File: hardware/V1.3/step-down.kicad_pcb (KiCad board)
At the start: 2 copper layers, 40 x 40 mm, 37 parts, among them J1 STACK-UP-HIGH, J2 STACK-UP-HIGH, P1 Black, P2 Green, Q1 FDS8449, U1 ZXCT1086, U2 AOZ1212, U3 DRILL, U4 DRILL, U5 DRILL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

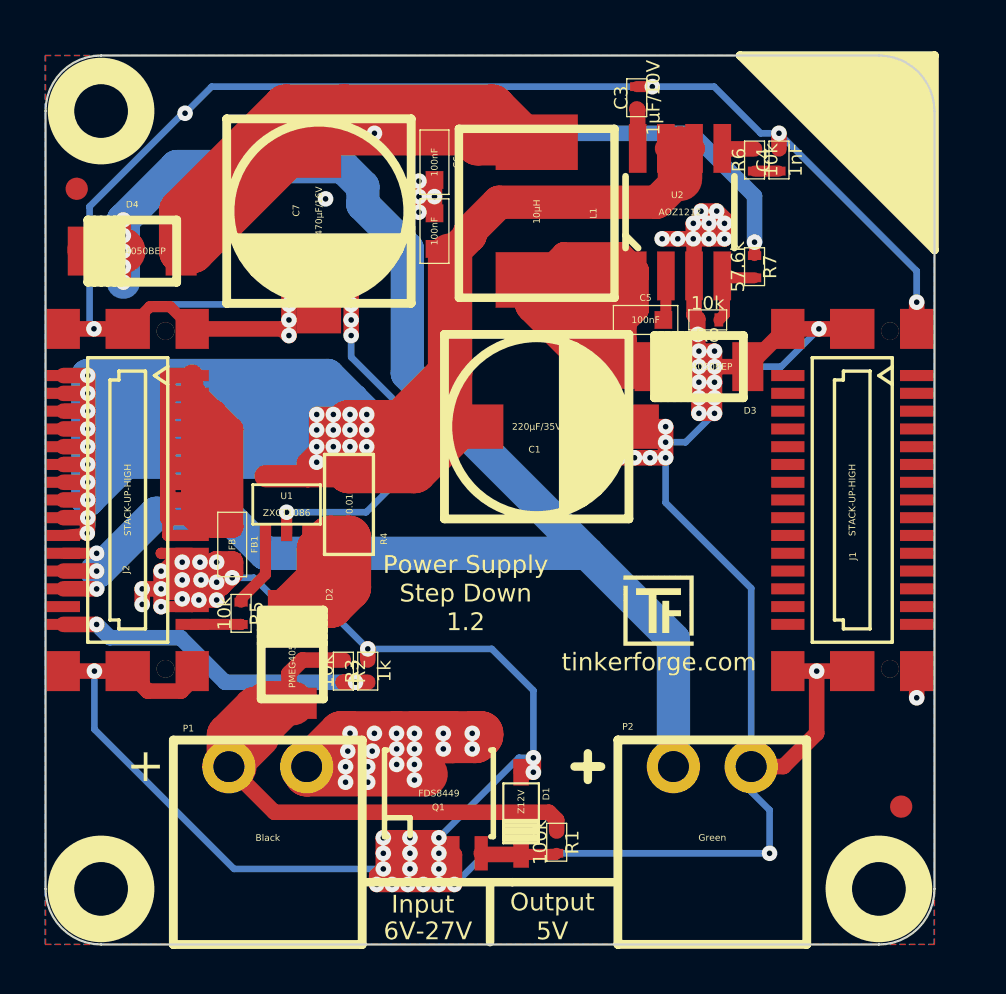
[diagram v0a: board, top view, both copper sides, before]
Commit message: updated version of new prototype, change current sensor, add filtering, not finished
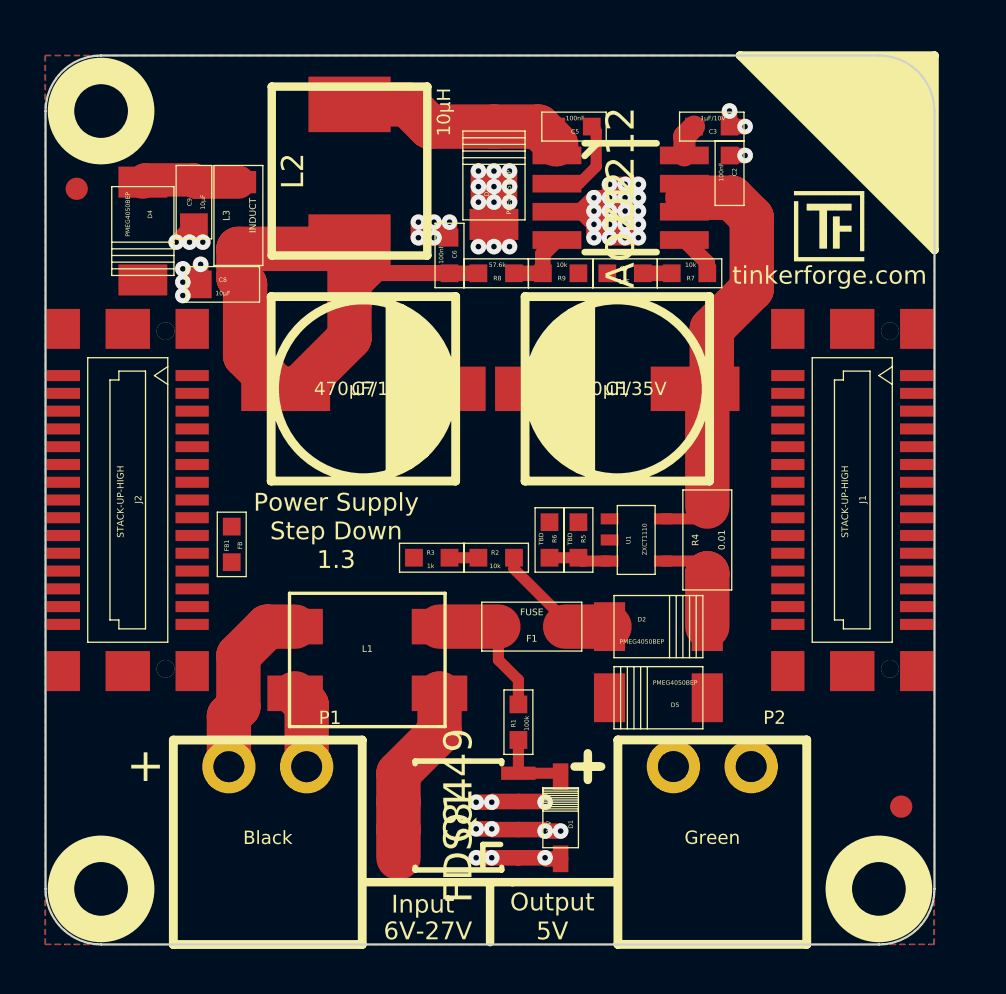
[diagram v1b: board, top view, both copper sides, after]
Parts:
- added C8: 10µF, kicad-libraries:0805, F.Cu at (138.6, 93.9)
- added C9: 10µF, kicad-libraries:0805, F.Cu at (137.3, 90.2)
- added D5: PMEG4050BEP, kicad-libraries:SOD-128, F.Cu at (158.2, 112.5)
- added F1: FUSE, kicad-libraries:1206, F.Cu at (152.5, 109.3)
- added L2: 10µH, kicad-libraries:SRP7030, F.Cu at (144.3, 88.9)
- added L3: INDUCT, kicad-libraries:1206, F.Cu at (139.3, 90.8)
- added R9: 10k, kicad-libraries:0603, F.Cu at (153.8, 93.4)
- C1, C7: footprint ELKO_83 -> kicad-libraries:ELKO_83
- C2, C5, C6, FB1: footprint 0603 -> kicad-libraries:0603
- C3, C4, R1, R2, R3: footprint 0402 -> kicad-libraries:0603
- D1: footprint SOD-123 -> kicad-libraries:SOD-123
- D2, D3, D4: footprint SOD-128 -> kicad-libraries:SOD-128
- J1, J2: footprint BTB08-ACS-TOP -> kicad-libraries:BTB08-ACS-TOP
- L1: value 10µH -> ICM2824ER301V; footprint SRP7030 -> kicad-libraries:ICM2824
- P1, P2: footprint OQ_2P -> kicad-libraries:OQ_2P
- Q1: footprint SOIC-8-MOSFET -> kicad-libraries:SOIC-8-MOSFET
- R4: footprint 1206 -> kicad-libraries:1206
- R5, R6: value 10k -> TBD; footprint 0402 -> kicad-libraries:0603
- R7: value 57.6k -> 10k; footprint 0402 -> kicad-libraries:0603
- R8: value 10k -> 57.6k; footprint 0402 -> kicad-libraries:0603
- U1: value ZXCT1086 -> ZXCT1110; footprint SOT23-5 -> kicad-libraries:SOT23-5
- U2: footprint SO-8 -> kicad-libraries:SO-8
- U3, U4, U5, U6: footprint DRILL_NP -> kicad-libraries:DRILL_NP
- moved L1 21.6 mm to (145.1, 110.8), turned to 180 degrees
- moved R6 19.4 mm to (153.3, 105.4)
- moved Ref** 18.9 mm to (164.3, 89.7)
- moved D2 16.5 mm to (158.2, 109.3), turned to 180 degrees
- moved R4 16.2 mm to (160.4, 105.4)
- moved U1 15.8 mm to (157.2, 105.4), turned to 270 degrees
- moved R5 15.5 mm to (154.6, 105.4), turned to 90 degrees
- moved C2 13.5 mm to (161.4, 88.9)
- moved D3 12.6 mm to (150.8, 89.0), turned to 270 degrees
- moved R8 9.75 mm to (150.9, 93.4), turned to 0 degrees
- moved C5 9.28 mm to (154.4, 86.8)
- moved C4 8.60 mm to (156.7, 93.4), turned to 180 degrees
- moved R2 8.56 mm to (150.9, 106.2), turned to 180 degrees
- moved C7 8.24 mm to (144.9, 98.6), turned to 180 degrees
- moved R3 5.86 mm to (148.0, 106.2), turned to 180 degrees
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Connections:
- C4 pad 1: N-000015 -> Net-(C4-Pad1)
- C5 pad 1: N-000005 -> Net-(C5-Pad1)
- C6 pad 1: N-000007 -> Net-(C6-Pad1)
- C7 pad 1: N-000007 -> Net-(C6-Pad1)
- D2 pad 1: N-000017 -> Net-(D2-Pad1)
- D2 pad 2: N-000002 -> Net-(D2-Pad2)
- D3 pad 2: N-000005 -> Net-(C5-Pad1)
- D4 pad 1: N-000007 -> Net-(C9-Pad1)
- L1 pad 1: N-000005 -> Net-(L1-Pad1)
- L1 pad 2: N-000007 -> Net-(L1-Pad2)
- P1 pad 1: N-000017 -> Net-(L1-Pad3)
- P1 pad 2: N-000012 -> Net-(L1-Pad2)
- P2 pad 1: +5V -> Net-(D5-Pad2)
- Q1 pad D: N-000012 -> Net-(L1-Pad1)
- R1 pad 1: N-000017 -> Net-(F1-Pad1)
- R2 pad 1: N-000017 -> Net-(D2-Pad1)
- R4 pad 2: N-000002 -> Net-(D2-Pad2)
- R5 pad 1: N-000004 -> Net-(R5-Pad1)
- R5 pad 2: CURRENT -> GND
- R6 pad 1: N-000015 -> Net-(R5-Pad1)
- R6 pad 2: N-000016 -> CURRENT
- R7 pad 1: N-000007 -> Net-(C4-Pad1)
- R7 pad 2: N-000010 -> Net-(R7-Pad2)
- R8 pad 1: N-000010 -> Net-(C6-Pad1)
- R8 pad 2: GND -> Net-(R8-Pad2)
- U1 pad 1: N-000004 -> (no net)
- U1 pad 3: N-000002 -> Net-(R5-Pad1)
- U1 pad 4: VPP -> Net-(D2-Pad2)
- U2 pad 1: N-000005 -> Net-(C5-Pad1)
- U2 pad 4: N-000010 -> Net-(R8-Pad2)
- U2 pad 5: N-000016 -> Net-(R7-Pad2)
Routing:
- net GND: track 289.4 -> 51.8 mm, vias 92 -> 57
- net VPP: track 158.0 -> 22.8 mm, vias 23 -> 0
- net +5V: track 84.6 -> 0.00 mm, vias 8 -> 0
- net N-000007: track 68.3 -> 0.00 mm, vias 2 -> 0
- net N-000012: track 52.6 -> 0.00 mm, vias 19 -> 0
- net AGND: track 42.4 -> 0.00 mm
- net N-000017: track 36.1 -> 0.00 mm
- net Net-(C6-Pad1): track 0.00 -> 32.0 mm
- net N-000005: track 28.3 -> 0.00 mm
- net VOLTAGE: track 16.4 -> 1.30 mm, vias 2 -> 0
- net Net-(C5-Pad1): track 0.00 -> 14.2 mm
- net N-000002: track 11.7 -> 0.00 mm
- net Net-(L1-Pad3): track 0.00 -> 8.27 mm
- net Net-(L1-Pad1): track 0.00 -> 8.17 mm
- net Net-(F1-Pad1): track 0.00 -> 6.52 mm
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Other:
- board text added: "Power Supply Step Down 1.3"
- board text removed: "Power Supply Step Down 1.2"

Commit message: next routing test, vpp seems to be not routable
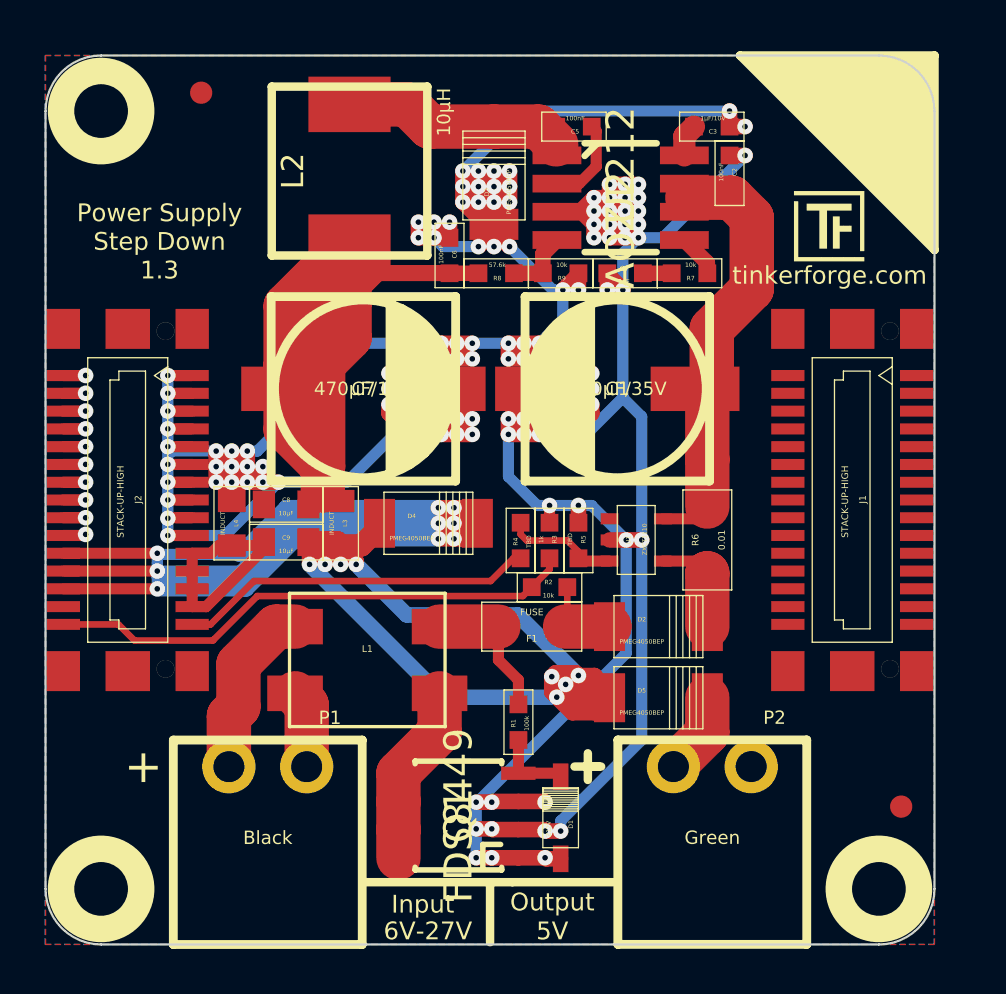
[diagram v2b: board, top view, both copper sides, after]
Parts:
- removed FB1: FB, kicad-libraries:0603
- added L4: INDUCT, kicad-libraries:0805, F.Cu at (139.0, 104.7)
- L3: footprint kicad-libraries:1206 -> kicad-libraries:0805
- R4: value 0.01 -> TBD; footprint kicad-libraries:1206 -> kicad-libraries:0603
- R6: value TBD -> 0.01; footprint kicad-libraries:0603 -> kicad-libraries:1206
- moved D4 18.4 mm to (147.8, 104.7), turned to 180 degrees
- moved C9 15.9 mm to (141.4, 105.5), turned to 180 degrees
- moved L3 14.6 mm to (143.9, 104.7), turned to 90 degrees
- moved C8 10.3 mm to (141.4, 103.8)
- moved R4 8.40 mm to (152.0, 105.4)
- moved R6 7.10 mm to (160.4, 105.4), turned to 270 degrees
- moved Fiducial_Mark 7.08 mm to (137.6, 85.3)
- moved R3 5.36 mm to (153.3, 105.4), turned to 90 degrees
- moved R2 2.74 mm to (153.3, 107.5)
- turned D5 to 180 degrees
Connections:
- C1 pad 2: GND -> AGND
- C2 pad 2: GND -> AGND
- C3 pad 2: GND -> AGND
- C4 pad 2: GND -> AGND
- C6 pad 2: GND -> AGND
- C7 pad 2: GND -> AGND
- C8 pad 2: GND -> AGND
- D1 pad 1: GND -> AGND
- D3 pad 1: GND -> AGND
- J1 pad EP: GND -> AGND
- J2 pad EP: GND -> AGND
- Q1 pad S: GND -> AGND
- R3 pad 2: GND -> AGND
- R4 pad 1: VPP -> Net-(R4-Pad1)
- R4 pad 2: Net-(D2-Pad2) -> CURRENT
- R5 pad 1: Net-(R5-Pad1) -> Net-(R4-Pad1)
- R5 pad 2: GND -> AGND
- R6 pad 1: Net-(R5-Pad1) -> VPP
- R6 pad 2: CURRENT -> Net-(D2-Pad2)
- R9 pad 2: GND -> AGND
- U1 pad 2: GND -> AGND
- U1 pad 3: Net-(R5-Pad1) -> Net-(R4-Pad1)
- U2 pad 3: GND -> AGND
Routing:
- net AGND: track 0.00 -> 233.4 mm, vias 0 -> 136
- net +5V: track 0.00 -> 71.6 mm, vias 0 -> 9
- net GND: track 51.8 -> 10.4 mm, vias 57 -> 0
- net Net-(C9-Pad1): track 4.38 -> 45.2 mm, vias 0 -> 8
- net VOLTAGE: track 1.30 -> 24.0 mm
- net CURRENT: track 0.00 -> 16.7 mm
- net Net-(C6-Pad1): track 32.0 -> 43.1 mm
- net VPP: track 22.8 -> 32.8 mm, vias 0 -> 10
- net Net-(R4-Pad1): track 0.00 -> 5.21 mm
- net Net-(D5-Pad2): track 0.00 -> 3.73 mm
- net Net-(R5-Pad1): track 2.76 -> 0.00 mm
- net Net-(D2-Pad1): track 6.05 -> 4.11 mm

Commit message: routing finished
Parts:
- moved Fiducial_Mark 0.53 mm to (137.1, 85.1)
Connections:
- P2 pad 2: GND -> AGND
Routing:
- net VPP: track 32.8 -> 141.9 mm, vias 10 -> 19
- net AGND: track 233.4 -> 301.4 mm, vias 136 -> 143
- net Net-(C6-Pad1): track 43.1 -> 50.2 mm
- net +5V: track 71.6 -> 72.6 mm, vias 9 -> 11
- added copper zone on B.Cu, net +5V
- added copper zone on F.Cu, net +5V
- added copper zone on B.Cu, net AGND
- added copper zone on F.Cu, net AGND
- added copper zone on B.Cu, net Net-(C9-Pad1)
- added copper zone on B.Cu, net VPP
- added copper zone on F.Cu, net VPP
- removed copper zone on B.Cu, net GND

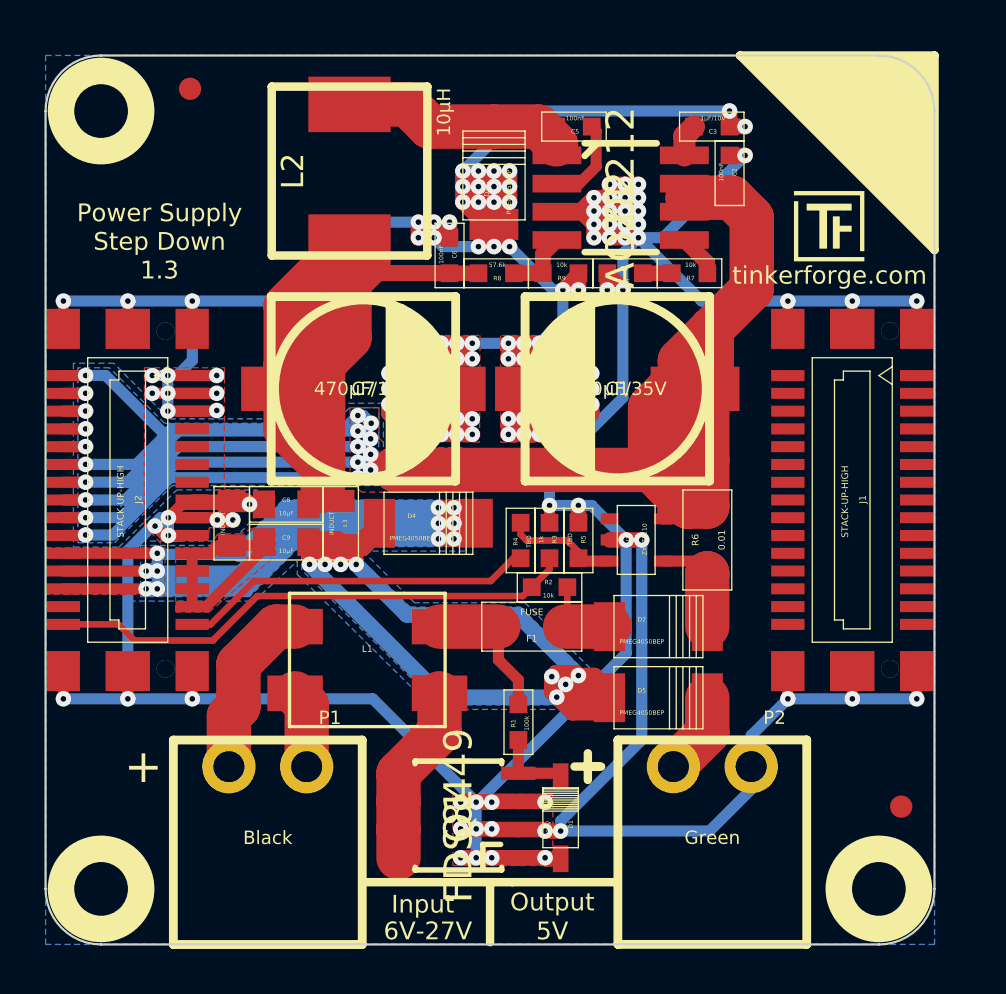
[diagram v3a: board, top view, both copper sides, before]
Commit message: change version 1.3, remove filters
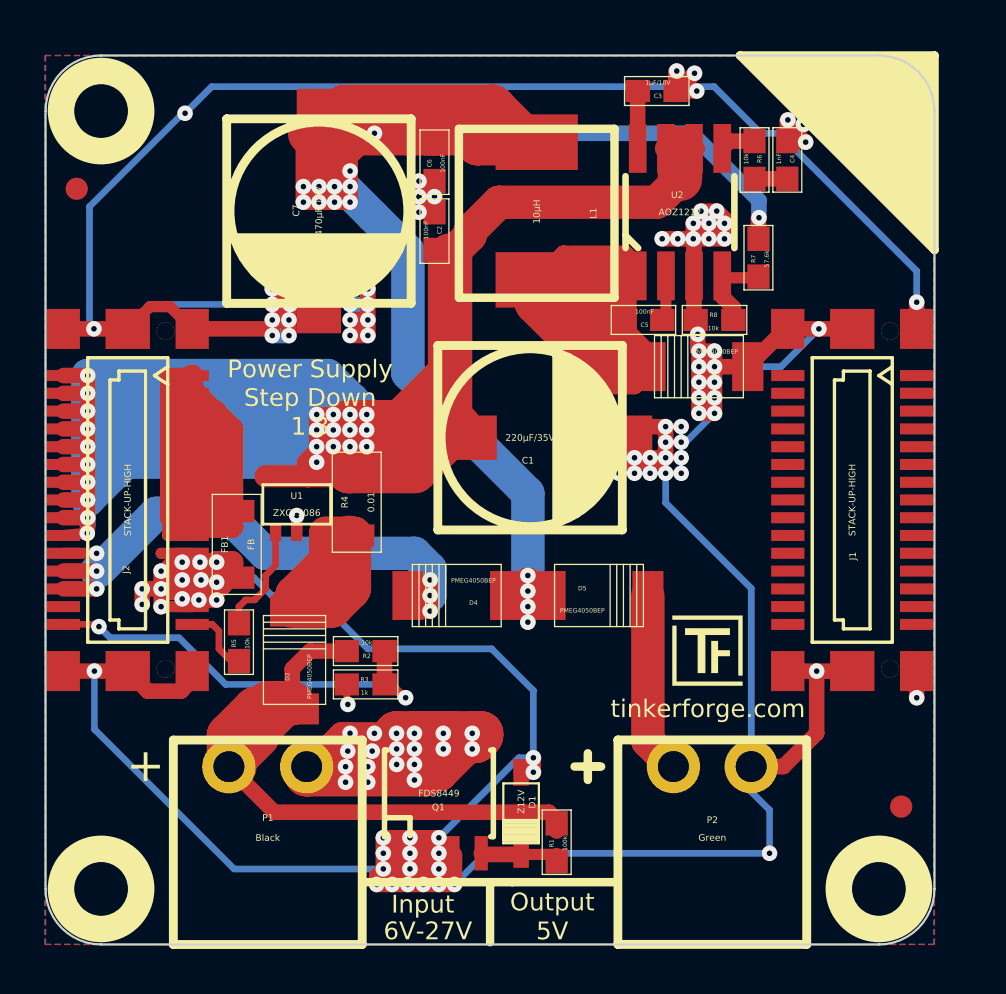
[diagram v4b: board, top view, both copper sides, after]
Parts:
- removed C8, C9: 10µF, kicad-libraries:0805
- removed F1: FUSE, kicad-libraries:1206
- removed L2: 10µH, kicad-libraries:SRP7030
- removed L3, L4: INDUCT, kicad-libraries:0805
- removed R9: 10k, kicad-libraries:0603
- added FB1: FB, kicad-libraries:1206, F.Cu at (139.2, 105.6)
- C1, C7: footprint kicad-libraries:ELKO_83 -> ELKO_83
- C2, C3, C4, C5, C6, R1, R2, R3: footprint kicad-libraries:0603 -> 0603E
- D1: footprint kicad-libraries:SOD-123 -> SOD-123
- D2, D3, D4, D5: footprint kicad-libraries:SOD-128 -> SOD-128
- J1, J2: footprint kicad-libraries:BTB08-ACS-TOP -> BTB08-ACS-TOP
- L1: value ICM2824ER301V -> 10µH; footprint kicad-libraries:ICM2824 -> SRP7030
- P1, P2: footprint kicad-libraries:OQ_2P -> OQ_2P
- Q1: footprint kicad-libraries:SOIC-8-MOSFET -> SOIC-8-MOSFET
- R4: value TBD -> 0.01; footprint kicad-libraries:0603 -> kicad-libraries:1206
- R5: value TBD -> 10k; footprint kicad-libraries:0603 -> 0603E
- R6: value 0.01 -> 10k; footprint kicad-libraries:1206 -> 0603E
- R7: value 10k -> 57.6k; footprint kicad-libraries:0603 -> 0603E
- R8: value 57.6k -> 10k; footprint kicad-libraries:0603 -> 0603E
- U1: value ZXCT1110 -> ZXCT1086; footprint kicad-libraries:SOT23-5 -> SOT23-5
- U2: footprint kicad-libraries:SO-8 -> SO-8
- U3, U4, U5, U6: footprint kicad-libraries:DRILL_NP -> DRILL_NP
- moved L1 21.6 mm to (152.7, 90.6), turned to 90 degrees
- moved Ref** 19.9 mm to (158.8, 108.8)
- moved R6 17.2 mm to (162.5, 88.3), turned to 90 degrees
- moved D2 16.4 mm to (141.8, 110.8), turned to 270 degrees
- moved R5 15.9 mm to (139.3, 110.0), turned to 270 degrees
- moved U1 15.4 mm to (141.9, 103.8), turned to 0 degrees
- moved C2 13.5 mm to (148.1, 91.5)
- moved D3 12.6 mm to (160.0, 97.6), turned to 0 degrees
- moved R3 10.5 mm to (145.0, 111.9), turned to 180 degrees
- moved R8 10.0 mm to (160.7, 95.5), turned to 180 degrees
- moved C5 9.24 mm to (157.5, 95.5)
- moved C4 8.91 mm to (164.0, 88.3), turned to 90 degrees
- moved R2 8.76 mm to (145.0, 110.4), turned to 0 degrees
- moved C7 8.24 mm to (142.9, 90.6), turned to 90 degrees
- moved R4 7.57 mm to (144.6, 103.7)
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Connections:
- C1 pad 2: AGND -> GND
- C2 pad 2: AGND -> GND
- C3 pad 2: AGND -> GND
- C4 pad 2: AGND -> GND
- C6 pad 2: AGND -> GND
- C7 pad 2: AGND -> GND
- D1 pad 1: AGND -> GND
- D3 pad 1: AGND -> GND
- D4 pad 1: Net-(C9-Pad1) -> Net-(C6-Pad1)
- D5 pad 1: Net-(C9-Pad1) -> Net-(C6-Pad1)
- J1 pad EP: AGND -> GND
- J2 pad EP: AGND -> GND
- L1 pad 1: Net-(L1-Pad1) -> Net-(C5-Pad1)
- L1 pad 2: Net-(L1-Pad2) -> Net-(C6-Pad1)
- P1 pad 1: Net-(L1-Pad3) -> Net-(D2-Pad1)
- P1 pad 2: Net-(L1-Pad2) -> Net-(P1-Pad2)
- P2 pad 2: AGND -> GND
- Q1 pad D: Net-(L1-Pad1) -> Net-(P1-Pad2)
- Q1 pad S: AGND -> GND
- R1 pad 1: Net-(F1-Pad1) -> Net-(D2-Pad1)
- R3 pad 2: AGND -> GND
- R4 pad 1: Net-(R4-Pad1) -> VPP
- R4 pad 2: CURRENT -> Net-(D2-Pad2)
- R5 pad 1: Net-(R4-Pad1) -> Net-(R5-Pad1)
- R5 pad 2: AGND -> CURRENT
- R6 pad 1: VPP -> Net-(C4-Pad1)
- R6 pad 2: Net-(D2-Pad2) -> Net-(R6-Pad2)
- R7 pad 1: Net-(C4-Pad1) -> Net-(C6-Pad1)
- R8 pad 1: Net-(C6-Pad1) -> Net-(R7-Pad2)
- R8 pad 2: Net-(R8-Pad2) -> GND
- U1 pad 1: (no net) -> Net-(R5-Pad1)
- U1 pad 2: AGND -> GND
- U1 pad 3: Net-(R4-Pad1) -> Net-(D2-Pad2)
- U1 pad 4: Net-(D2-Pad2) -> VPP
- U2 pad 3: AGND -> GND
- U2 pad 4: Net-(R8-Pad2) -> Net-(R7-Pad2)
- U2 pad 5: Net-(R7-Pad2) -> Net-(R6-Pad2)
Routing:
- net GND: track 10.4 -> 308.2 mm, vias 0 -> 119
- net AGND: track 301.4 -> 52.1 mm, vias 143 -> 0
- net Net-(P1-Pad2): track 0.00 -> 55.9 mm, vias 0 -> 19
- net Net-(C6-Pad1): track 50.2 -> 102.4 mm, vias 0 -> 15
- net Net-(C9-Pad1): track 45.2 -> 0.00 mm, vias 8 -> 0
- net +5V: track 72.6 -> 29.4 mm, vias 11 -> 6
- net Net-(D2-Pad1): track 4.11 -> 36.2 mm
- net Net-(C5-Pad1): track 14.2 -> 37.4 mm
- net VPP: track 141.9 -> 161.8 mm, vias 19 -> 23
- net CURRENT: track 16.7 -> 3.26 mm
- net Net-(L1-Pad1): track 8.17 -> 0.00 mm
- net Net-(L1-Pad3): track 8.03 -> 0.00 mm
- net Net-(D2-Pad2): track 4.63 -> 12.6 mm
- net Net-(F1-Pad1): track 6.52 -> 0.00 mm
- net Net-(R4-Pad1): track 5.21 -> 0.00 mm
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- added copper zone on B.Cu, net GND
- removed copper zone on B.Cu, net +5V
- removed copper zone on F.Cu, net +5V
- removed copper zone on B.Cu, net AGND
- removed copper zone on F.Cu, net AGND
- removed copper zone on B.Cu, net Net-(C9-Pad1)
- removed copper zone on B.Cu, net VPP
- removed copper zone on F.Cu, net VPP
